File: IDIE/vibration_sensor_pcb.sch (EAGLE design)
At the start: 63 parts, among them IC1 LORA-E5, IC2 STM32L071KBT6, IC3 FXLS8974CFR3, IC4 FXLS8971CFR1, IC5 DRV5032FBLPGM, IC6 FT234XD-T, J1 217182-0001, Q2 SI2305B-TP, Y1 ABS06-32.768KHZ-9-1-T

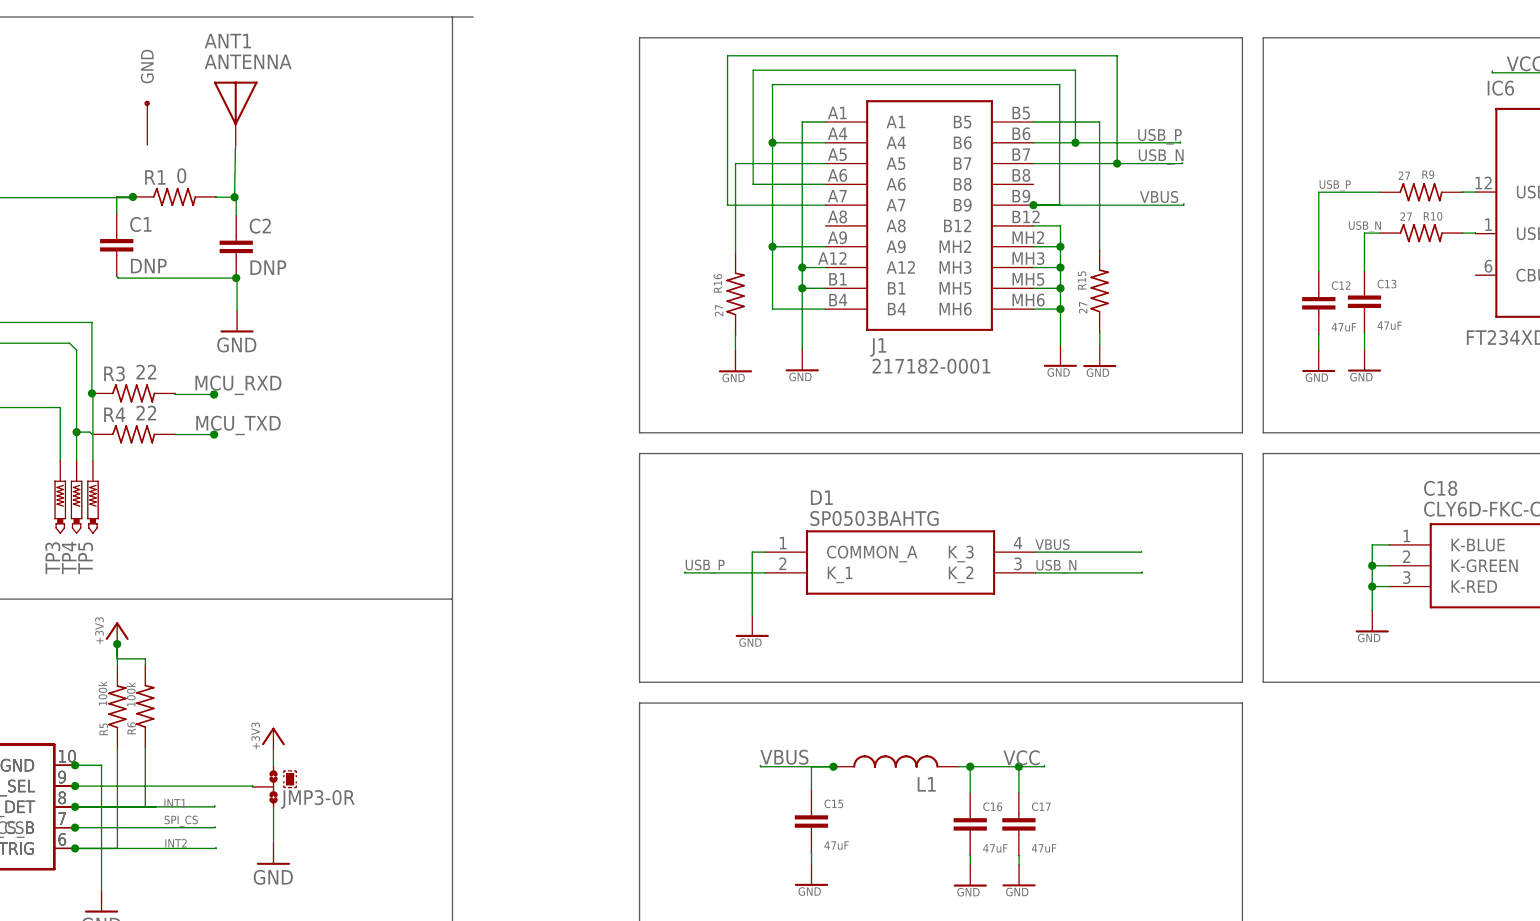
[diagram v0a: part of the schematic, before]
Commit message: UPDATE orden de pcb y reglas de diseño
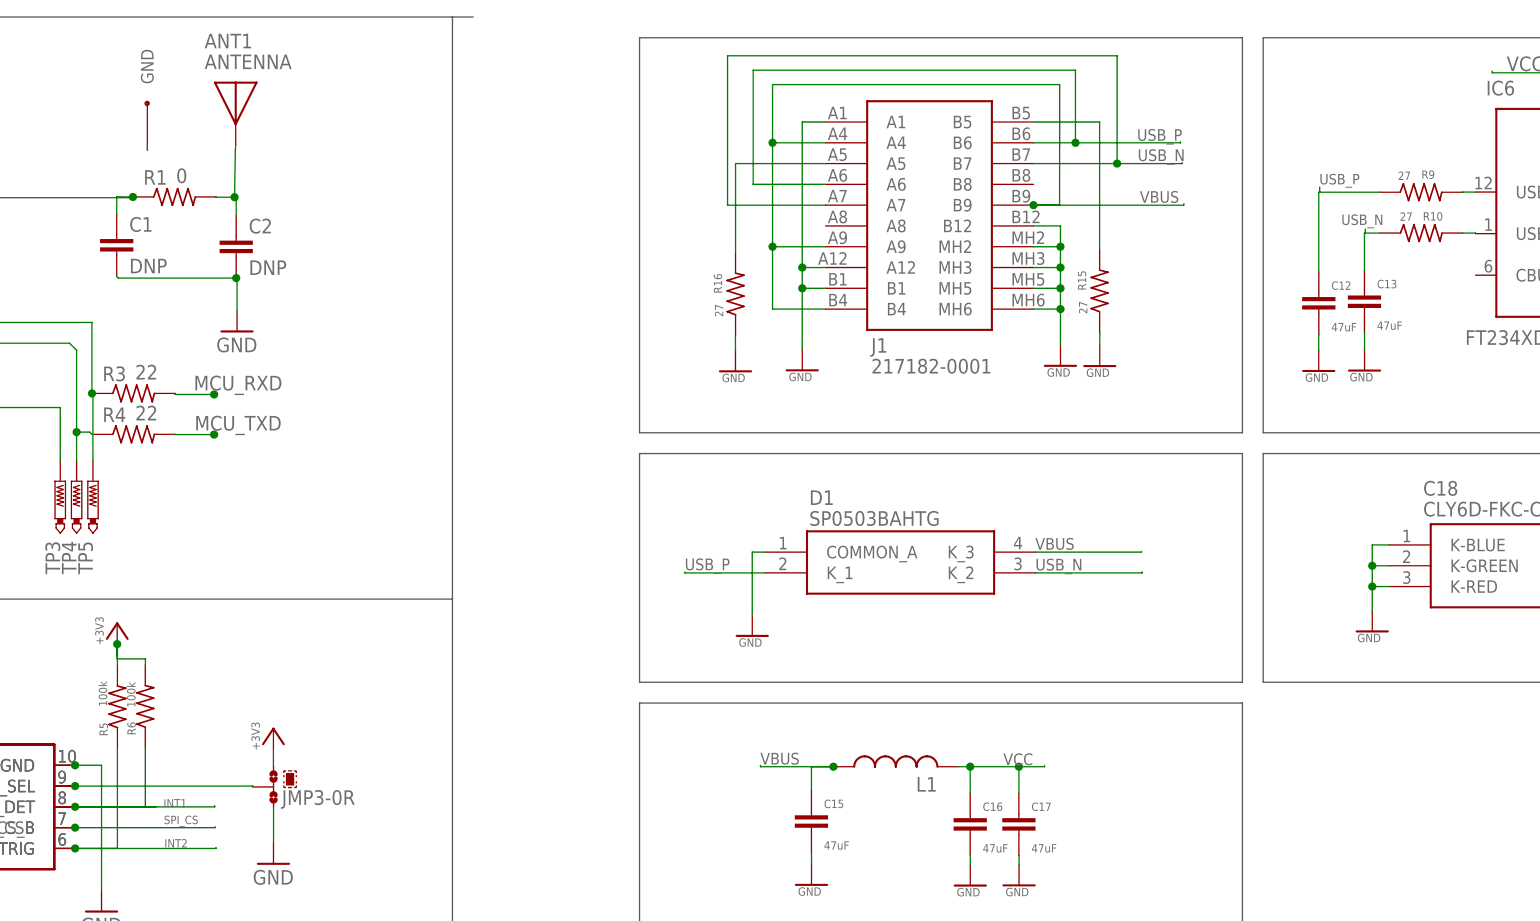
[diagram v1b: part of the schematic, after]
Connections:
- net GND: now also ANT1.GND
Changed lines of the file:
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@@
 <setting verticaltext="up"/>
 </settings>
-<grid distance="0.1" unitdist="inch" unit="inch" style="lines" multiple="1" display="no" altdistance="0.01" altunitdist="inch" altunit="inch"/>
+<grid distance="0.01" unitdist="mm" unit="mm" style="lines" multiple="1" display="no" altdistance="1" altunitdist="mm" altunit="mm"/>
 <layers>
 <layer number="1" name="Top" color="4" fill="1" visible="no" active="no"/>
@@
 <junction x="361.3" y="103.13"/>
 </segment>
+<segment>
+<pinref part="ANT1" gate="G$1" pin="GND"/>
+<wire x1="211.64" y1="157.08" x2="211.64" y2="156.46" width="0.1524" layer="91"/>
+<wire x1="211.64" y1="156.46" x2="211.67" y2="156.46" width="0.1524" layer="91"/>
+</segment>
 </net>
 <net name="+3V3" class="0">
@@
 <net name="USB_N" class="0">
 <segment>
-<pinref part="C13" gate="G$1" pin="1"/>
-<pinref part="R10" gate="G$1" pin="1"/>
-<wire x1="360.35" y1="141.74" x2="360.35" y2="146.32" width="0.1524" layer="91"/>
-<wire x1="360.35" y1="146.32" x2="362.21" y2="146.32" width="0.1524" layer="91"/>
-<label x="358.34" y="146.73" size="1.016" layer="95"/>
-</segment>
-<segment>
 <pinref part="D1" gate="G$1" pin="K_2"/>
 <wire x1="320.18" y1="104.8" x2="333.18" y2="104.8" width="0.1524" layer="91"/>
 <wire x1="333.18" y1="104.8" x2="333.18" y2="104.92" width="0.1524" layer="91"/>
-<label x="320.13" y="105.1" size="1.27" layer="95"/>
+<label x="320.13" y="105.1" size="1.4224" layer="95"/>
 </segment>
 <segment>
@@
 <junction x="330.13" y="154.81"/>
 </segment>
+<segment>
+<pinref part="R10" gate="G$1" pin="1"/>
+<wire x1="362.21" y1="146.32" x2="360.47" y2="146.32" width="0.1524" layer="91"/>
+<wire x1="360.47" y1="146.32" x2="360.46" y2="146.32" width="0.1524" layer="91"/>
+<wire x1="360.46" y1="146.32" x2="360.46" y2="146.81" width="0.1524" layer="91"/>
+<label x="357.51" y="147.31" size="1.27" layer="95"/>
+<pinref part="C13" gate="G$1" pin="1"/>
+<wire x1="360.35" y1="141.74" x2="360.35" y2="146.32" width="0.1524" layer="91"/>
+<wire x1="360.35" y1="146.32" x2="360.46" y2="146.32" width="0.1524" layer="91"/>
+</segment>
 </net>
 <net name="USB_P" class="0">
-<segment>
-<pinref part="R9" gate="G$1" pin="1"/>
-<pinref part="C12" gate="G$1" pin="1"/>
-<wire x1="362.18" y1="151.31" x2="354.77" y2="151.31" width="0.1524" layer="91"/>
-<wire x1="354.77" y1="151.31" x2="354.77" y2="141.55" width="0.1524" layer="91"/>
-<label x="354.76" y="151.74" size="1.016" layer="95"/>
-</segment>
 <segment>
 <pinref part="D1" gate="G$1" pin="K_1"/>
 <wire x1="287.16" y1="104.8" x2="277.31" y2="104.8" width="0.1524" layer="91"/>
 <wire x1="277.31" y1="104.8" x2="277.31" y2="104.89" width="0.1524" layer="91"/>
-<label x="277.29" y="105.13" size="1.27" layer="95"/>
+<label x="277.29" y="105.13" size="1.4224" layer="95"/>
 </segment>
 <segment>
@@
 <junction x="325.04" y="157.35"/>
 </segment>
+<segment>
+<pinref part="R9" gate="G$1" pin="1"/>
+<wire x1="362.18" y1="151.31" x2="354.89" y2="151.31" width="0.1524" layer="91"/>
+<wire x1="354.89" y1="151.31" x2="354.88" y2="151.31" width="0.1524" layer="91"/>
+<wire x1="354.88" y1="151.31" x2="354.88" y2="151.94" width="0.1524" layer="91"/>
+<label x="354.83" y="152.27" size="1.27" layer="95"/>
+<pinref part="C12" gate="G$1" pin="1"/>
+<wire x1="354.77" y1="141.55" x2="354.77" y2="151.31" width="0.1524" layer="91"/>
+<wire x1="354.77" y1="151.31" x2="354.88" y2="151.31" width="0.1524" layer="91"/>
+</segment>
 </net>
 <net name="VBUS" class="0">
@@
 <wire x1="320.18" y1="107.34" x2="333.11" y2="107.34" width="0.1524" layer="91"/>
 <wire x1="333.11" y1="107.34" x2="333.11" y2="107.42" width="0.1524" layer="91"/>
-<label x="320.13" y="107.63" size="1.27" layer="95"/>
+<label x="320.13" y="107.63" size="1.4224" layer="95"/>
 </segment>
 <segment>
@@
 <wire x1="286.55" y1="81.12" x2="286.55" y2="81.29" width="0.1524" layer="91"/>
 <junction x="295.47" y="81.12"/>
-<label x="286.53" y="81.39" size="1.778" layer="95"/>
+<label x="286.53" y="81.39" size="1.4224" layer="95"/>
 </segment>
 <segment>
@@
 <wire x1="312.18" y1="77.88" x2="312.18" y2="81.12" width="0.1524" layer="91"/>
 <junction x="312.18" y="81.12"/>
-<label x="316.22" y="81.32" size="1.778" layer="95"/>
+<label x="316.22" y="81.32" size="1.4224" layer="95"/>
 <pinref part="C17" gate="G$1" pin="1"/>
 <wire x1="318.13" y1="77.88" x2="318.13" y2="81.12" width="0.1524" layer="91"/>

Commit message: ADD & UPDATE documentacion, modelado 3d y poco ruteo
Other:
- note added: "Diodo Protexion"
- note added: "Filtro"
- note added: "Filtro Bus"
- note added: "Led RGB"
- note added: "Modulo LoRa"
- note added: "Modulo Serial"
- note added: "Procesador"
- note added: "Puntos Guia"
- note added: "SANTIAGO CORTÉS TOVAR ANTHONY DE JESUS G"
- note added: "Selectores de uso"
- note added: "Sensor Efecto Tunel"
- note added: "Sensor Triaxial"
- note added: "Socket y protección"
- note added: "USB type C"
- note removed: "ESCUELA COLOMBIANA DE INGENIERIA"
- moved on the sheet: ANT1, C1, C10, C11, C12, C13, C14, C15, C16, C17, C18, C2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

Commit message: UPDATE schematic
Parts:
- removed D1: SP0503BAHTG, SamacSys_Parts:SP0503BAHTG
- added IC7: USBLC6-2SC6, SamacSys_Parts:USBLC6-2SC6
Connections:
- removed net SCL: JMP2-0R.3
- removed net SDA: JMP1-0R.3
- new net N$10: IC7.I/O2_1
- new net N$3: IC7.I/O1_2
- new net N$4: IC7.I/O2_2
- new net N$7: IC7.I/O1_1
- net GND: now also IC7.GND; no longer D1.COMMON_A
- net I2C_SCL: now also JMP2-0R.3
- net I2C_SDA: now also JMP1-0R.3
- net USB_N: no longer D1.K_2
- net USB_P: no longer D1.K_1
- net VBUS: now also IC7.VBUS; no longer D1.K_3
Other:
- note removed: "Diodo Protexion"
- note removed: "Filtro"
- note removed: "Filtro Bus"
- note removed: "Led RGB"
- note removed: "Modulo LoRa"
- note removed: "Modulo Serial"
- note removed: "Procesador"
- note removed: "Puntos Guia"
- note removed: "Selectores de uso"
- note removed: "Sensor Efecto Tunel"
- note removed: "Sensor Triaxial"
- note removed: "Socket y protección"
- note removed: "USB type C"
- moved on the sheet: ANT1, C1, C10, C11, C12, C13, C14, C15, C16, C17, C18, C2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

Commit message: UPDATE schematic and PCB route
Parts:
- added C19: 1uF, rcl:C-EUC0603
- added C20: 0.1uF, rcl:C-EUC0603
- added C21: 12.5uF, rcl:C-EUC0603
- added JP1: (no value), pinhead:PINHD-2X3
- added R20, R21: 4.7k, rcl:R-US_R0603
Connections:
- net N$1 renamed INTF_SEL
- net N$9 renamed RESET#
- removed net N$10: IC7.I/O2_1
- removed net N$3: IC7.I/O1_2
- removed net N$4: IC7.I/O2_2
- removed net N$7: IC7.I/O1_1
- removed net PA11: IC2.PA11
- removed net PA12: IC2.PA12
- removed net PA15: IC2.PA15
- new net GND1: C20.2
- new net N$2: JP1.2
- new net NRST: JP1.4
- new net USBC_N: IC7.I/O2_1, J1.A7, J1.B7
- new net USBC_P: IC7.I/O1_1, J1.A6, J1.B6
- net +3V3: now also C19.1, C20.1, JP1.1, R20.2, R21.2
- net BOOT: now also C21.1, IC2.NRST
- net GND: now also C19.2, C21.2, IC2.BOOT0, JP1.6
- net I2C_SCL: now also R21.1
- net I2C_SDA: now also R20.1
- net INT1: now also IC2.PA12
- net INT2: now also IC2.PA15
- net MCU_SWCLK: now also JP1.5
- net MCU_SWDIO: now also JP1.3
- net MD_RST: now also IC2.PA11
- net USB_N: now also IC7.I/O2_2; no longer J1.A7, J1.B7
- net USB_P: now also IC7.I/O1_2; no longer J1.A6, J1.B6
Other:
- moved on the sheet: C10, C11, C12, C13, C14, C15, C16, C17, C8, C9, FD1, FD2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

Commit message: UPDATE pcb schematic
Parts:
- removed Y1: ABS06-32.768KHZ-9-1-T, SamacSys_Parts:ABS06-32.768KHZ-9-1-T
- added CRISTAL: CRISTAL-32.768KHZ-9-1-T, SamacSys_Parts:CRISTAL-32.768KHZ-9-1-T
- added INT1, INT2, SCL/SCLK, SDA/MOSI, SPI_CS, SPI_MISO: PTR1TP11R, testpad:PTR1TP11R
- renumbered C18 to RGB, J1 to USB-C, Q2 to MOSFET, T1 to TRANSISTOR, TP1 to SWCLK, TP2 to SWDIO, TP3 to BOOT, TP4 to MCU_TXD, TP5 to MCU_RXD
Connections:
- net N$6 renamed GATE
- net BOOT: no longer C21.1, IC2.NRST
- net INT1: now also INT1.TP
- net INT2: now also INT2.TP
- net NRST: now also C21.1, IC2.NRST
- net OSC32_IN: now also CRISTAL.2; no longer Y1.2
- net OSC32_OUT: now also CRISTAL.1; no longer Y1.1
- net SCL/SCLK: now also SCL/SCLK.TP
- net SDA/MOSI: now also SDA/MOSI.TP
- net SPI_CS: now also SPI_CS.TP
- net SPI_MISO: now also SPI_MISO.TP
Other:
- note added: "CONVERSOR SERIAL"
- note added: "DIODO Y REGULACIÓN"
- note added: "FILTROS"
- note added: "HEADER PROGRAMACIÓN"
- note added: "JUMPERS"
- note added: "LED RGB"
- note added: "MICROCONTROLADOR"
- note added: "MODULO LORA-E5"
- note added: "PINES FABRICACIÓN"
- note added: "PROTECCION BATERIA"
- note added: "SENSOR EFECTO HALL"
- note added: "SENSOR TRIAXIAL"
- note added: "USB-C"
- moved on the sheet: C5, IC3, IC4, JMP3-0R, R2, R5, R6, R7
